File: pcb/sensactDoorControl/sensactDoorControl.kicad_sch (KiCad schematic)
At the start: 51 parts, among them J1 Conn_01x04, J10 Conn_01x06, J11 G19, J12 G23, J2 Conn_01x04, J3 Motor, J4 PROG, J5 Conn_01x04, J6 Conn_01x04, J7 G2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

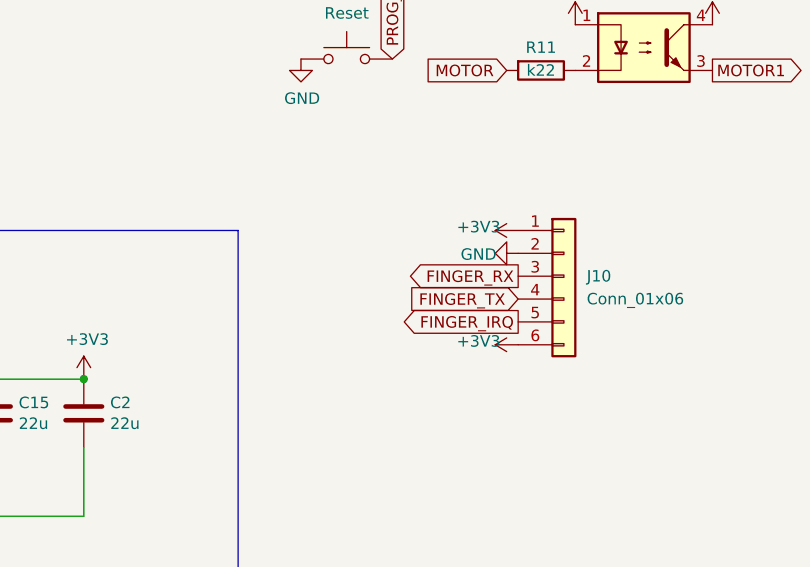
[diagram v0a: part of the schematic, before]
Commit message: sh connector with jumper
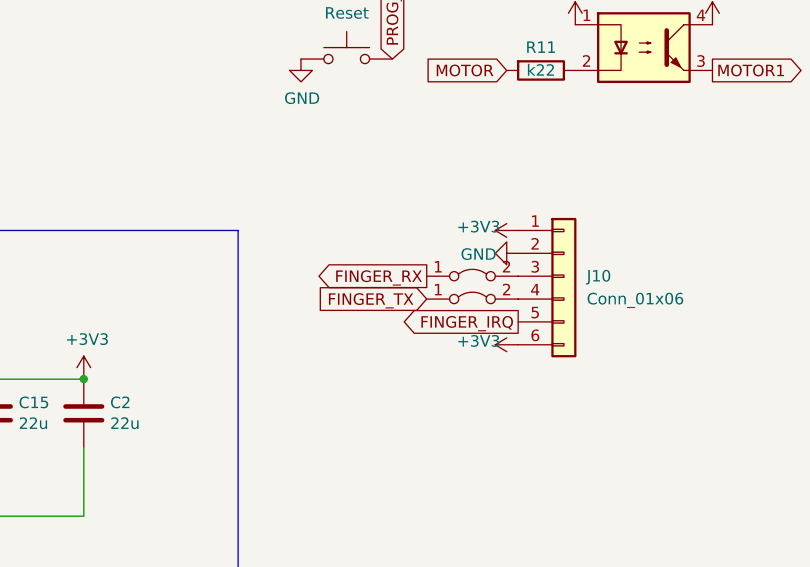
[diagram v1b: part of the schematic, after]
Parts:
- added JP1, JP2: Jumper_2_Bridged, Jumper:SolderJumper-2_P1.3mm_Bridged_RoundedPad1.0x1.5mm, symbol Jumper:Jumper_2_Bridged
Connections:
- net FINGER_RX: now also JP1.1 (A); no longer J10.3 (Pin_3)
- net FINGER_TX: now also JP2.1 (A); no longer J10.4 (Pin_4)
- new net: J10.3 (Pin_3), JP1.2 (B)
- new net: J10.4 (Pin_4), JP2.2 (B)
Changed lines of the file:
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@@
     )
   )
-  (global_label "FINGER_RX" (shape output) (at 153.67 151.13 180) (fields_autoplaced)
+  (global_label "FINGER_RX" (shape output) (at 143.51 151.13 180) (fields_autoplaced)
     (effects (font (size 1.27 1.27)) (justify right))
-    (property "Intersheetrefs" "${INTERSHEET_REFS}" (at 140.5248 151.13 0)
+    (property "Intersheetrefs" "${INTERSHEET_REFS}" (at 130.3648 151.13 0)
       (effects (font (size 1.27 1.27)) (justify right) hide)
     )
@@
     )
   )
-  (global_label "FINGER_TX" (shape input) (at 153.67 153.67 180) (fields_autoplaced)
+  (global_label "FINGER_TX" (shape input) (at 143.51 153.67 180) (fields_autoplaced)
     (effects (font (size 1.27 1.27)) (justify right))
-    (property "Intersheetrefs" "${INTERSHEET_REFS}" (at 140.8272 153.67 0)
+    (property "Intersheetrefs" "${INTERSHEET_REFS}" (at 130.6672 153.67 0)
       (effects (font (size 1.27 1.27)) (justify right) hide)
     )
@@
     )
   )
+  (symbol (lib_id "Jumper:Jumper_2_Bridged") (at 148.59 151.13 0) (unit 1)
+    (in_bom yes) (on_board yes) (dnp no) (fields_autoplaced)
+    (property "Reference" "JP1" (at 148.59 146.05 0)
+      (effects (font (size 1.27 1.27)) hide)
+    )
+    (property "Value" "Jumper_2_Bridged" (at 148.59 148.59 0)
+      (effects (font (size 1.27 1.27)) hide)
+    )
+    (property "Footprint" "Jumper:SolderJumper-2_P1.3mm_Bridged_RoundedPad1.0x1.5mm" (at 148.59 151.13 0)
+      (effects (font (size 1.27 1.27)) hide)
+    )
+    (property "Datasheet" "~" (at 148.59 151.13 0)
+      (effects (font (size 1.27 1.27)) hide)
+    )
+    (pin "2")
+    (pin "1")
+    (instances
+      (project "sensactDoorControl"
+        (path "/43f0baf2-6f79-4cf2-88c1-5a3cf0eb3b7b"
+          (reference "JP1") (unit 1)
+        )
+      )
+    )
+  )
   (symbol (lib_id "Device:R") (at 91.44 166.37 0) (unit 1)
     (in_bom yes) (on_board yes) (dnp no)
@@
         )
       )
+    )
+  )
+  (symbol (lib_id "Jumper:Jumper_2_Bridged") (at 148.59 153.67 0) (unit 1)
+    (in_bom yes) (on_board yes) (dnp no) (fields_autoplaced)
+    (property "Reference" "JP2" (at 148.59 148.59 0)
+      (effects (font (size 1.27 1.27)) hide)
+    )
+    (property "Value" "Jumper_2_Bridged" (at 148.59 151.13 0)
+      (effects (font (size 1.27 1.27)) hide)
+    )
+    (property "Footprint" "Jumper:SolderJumper-2_P1.3mm_Bridged_RoundedPad1.0x1.5mm" (at 148.59 153.67 0)
+      (effects (font (size 1.27 1.27)) hide)
+    )
+    (property "Datasheet" "~" (at 148.59 153.67 0)
+      (effects (font (size 1.27 1.27)) hide)
+    )
+    (pin "2")
+    (pin "1")
+    (instances
+      (project "sensactDoorControl"
+        (path "/43f0baf2-6f79-4cf2-88c1-5a3cf0eb3b7b"
+          (reference "JP2") (unit 1)
+        )
+      )

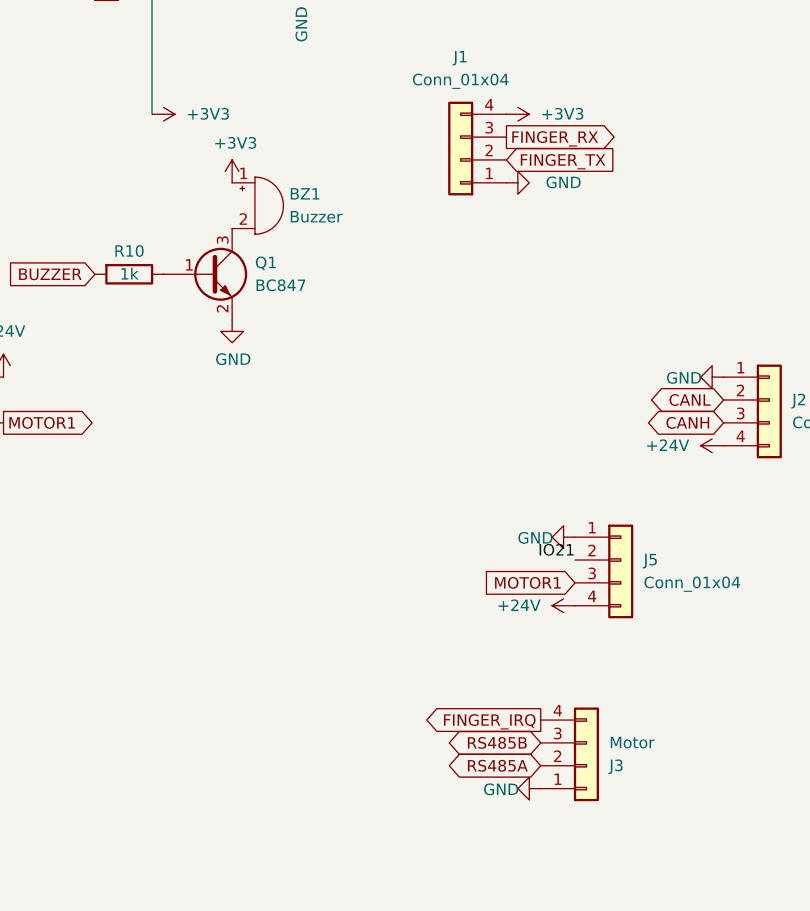
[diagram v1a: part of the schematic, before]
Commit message: Improved layout sensactDoorControl
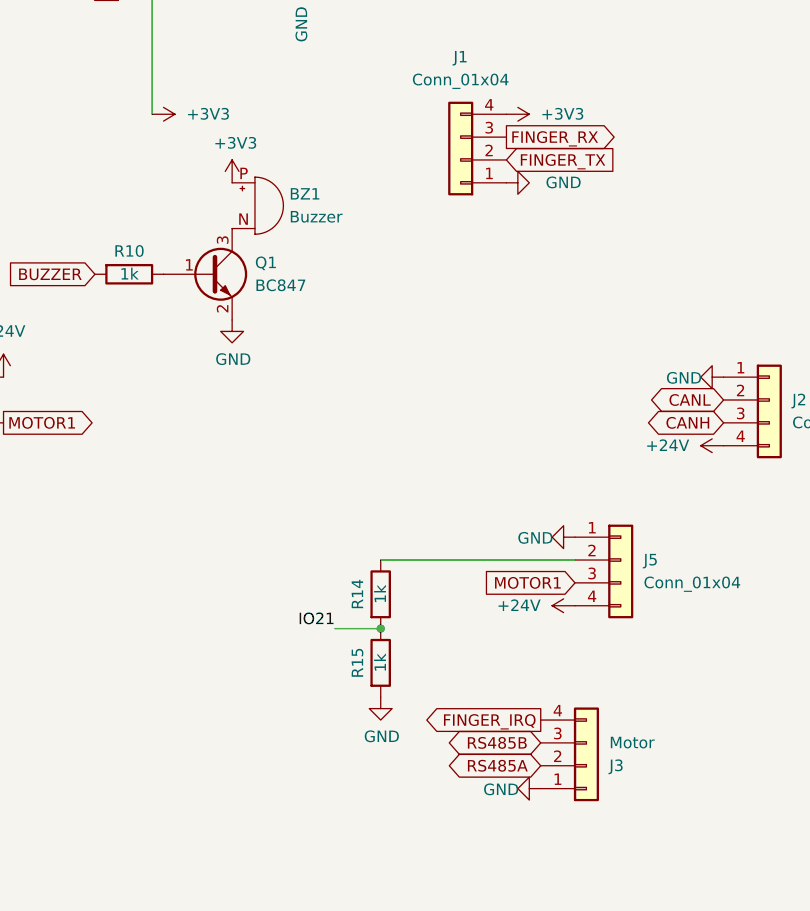
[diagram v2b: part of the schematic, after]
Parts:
- removed BZ1: Buzzer, Buzzer_Beeper:Buzzer_12x9.5RM7.6, symbol Device:Buzzer
- added BZ1: Buzzer, liebler_MECH:XDCR_CMT-7525-80-SMT-TR_handsolder, symbol liebler_MECH:Buzzer
- added R14, R15: 1k, Resistor_SMD:R_0805_2012Metric_Pad1.20x1.40mm_HandSolder, symbol Device:R
- JP1: value Jumper_2_Bridged -> RX
- JP2: value Jumper_2_Bridged -> TX
- SW1, SW2: footprint Button_Switch_SMD:SW_Push_1P1T_NO_6x6mm_H9.5mm -> liebler_MECH:SW_SPST_TL3342_smaller_handsolder
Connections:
- net +3V3: now also BZ1.P (+)
- net GND: now also R15.2
- net IO21: now also R14.2, R15.1; no longer J5.2 (Pin_2)
- net at Q1.3 (C): now also BZ1.N (-)
- new net: J5.2 (Pin_2), R14.1
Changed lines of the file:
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@@
   (junction (at 151.13 77.47) (diameter 0) (color 0 0 0 0)
+  )
+  (junction (at 217.17 151.13) (diameter 0) (color 0 0 0 0)
   )
   (junction (at 83.82 170.18) (diameter 0) (color 0 0 0 0)
@@
     (stroke (width 0) (type default))
   )
+  (wire (pts (xy 212.09 151.13) (xy 217.17 151.13))
+    (stroke (width 0) (type default))
+  )
   (wire (pts (xy 95.25 177.8) (xy 91.44 177.8))
     (stroke (width 0) (type default))
@@
   )
   (wire (pts (xy 95.25 170.18) (xy 95.25 177.8))
+    (stroke (width 0) (type default))
+  )
+  (wire (pts (xy 217.17 143.51) (xy 238.76 143.51))
     (stroke (width 0) (type default))
   )
@@
     (effects (font (size 1.27 1.27)) (justify right bottom))
   )
-  (label "IO21" (at 238.76 143.51 180) (fields_autoplaced)
+  (label "IO21" (at 212.09 151.13 180) (fields_autoplaced)
     (effects (font (size 1.27 1.27)) (justify right bottom))
   )
@@
         (path "/43f0baf2-6f79-4cf2-88c1-5a3cf0eb3b7b"
           (reference "R7") (unit 1)
-        )
-      )
-    )
-  )
-  (symbol (lib_id "Device:Buzzer") (at 203.2 104.14 0) (unit 1)
-    (in_bom yes) (on_board yes) (dnp no) (fields_autoplaced)
-    (property "Reference" "BZ1" (at 207.01 102.87 0)
-      (effects (font (size 1.27 1.27)) (justify left))
-    )
-    (property "Value" "Buzzer" (at 207.01 105.41 0)
-      (effects (font (size 1.27 1.27)) (justify left))
-    )
-    (property "Footprint" "Buzzer_Beeper:Buzzer_12x9.5RM7.6" (at 202.565 101.6 90)
-      (effects (font (size 1.27 1.27)) hide)
-    )
-    (property "Datasheet" "~" (at 202.565 101.6 90)
-      (effects (font (size 1.27 1.27)) hide)
-    )
-    (pin "1")
-    (pin "2")
-    (instances
-      (project "sensactDoorControl"
-        (path "/43f0baf2-6f79-4cf2-88c1-5a3cf0eb3b7b"
-          (reference "BZ1") (unit 1)
         )
       )
@@
     )
   )
+  (symbol (lib_id "Device:R") (at 217.17 154.94 0) (unit 1)
+    (in_bom yes) (on_board yes) (dnp no)
+    (property "Reference" "R15" (at 214.63 154.94 90)
+      (effects (font (size 1.27 1.27)))
+    )
+    (property "Value" "1k" (at 217.17 154.94 90)
+      (effects (font (size 1.27 1.27)))
+    )
+    (property "Footprint" "Resistor_SMD:R_0805_2012Metric_Pad1.20x1.40mm_HandSolder" (at 215.392 154.94 90)
+      (effects (font (size 1.27 1.27)) hide)
+    )
+    (property "Datasheet" "~" (at 217.17 154.94 0)
+      (effects (font (size 1.27 1.27)) hide)
+    )
+    (pin "1")
+    (pin "2")
+    (instances
+      (project "sensactDoorControl"
+        (path "/43f0baf2-6f79-4cf2-88c1-5a3cf0eb3b7b"
+          (reference "R15") (unit 1)
+        )
+      )
+    )
+  )
   (symbol (lib_id "power:GND") (at 200.66 116.84 0) (unit 1)
     (in_bom yes) (on_board yes) (dnp no)
@@
       (effects (font (size 1.27 1.27)))
     )
-    (property "Footprint" "Button_Switch_SMD:SW_Push_1P1T_NO_6x6mm_H9.5mm" (at 134.62 121.92 0)
+    (property "Footprint" "liebler_MECH:SW_SPST_TL3342_smaller_handsolder" (at 134.62 121.92 0)
       (effects (font (size 1.27 1.27)) hide)
     )
@@
       (effects (font (size 1.27 1.27)) hide)
     )
-    (property "Value" "Jumper_2_Bridged" (at 148.59 148.59 0)
+    (property "Value" "RX" (at 148.59 148.59 0)
       (effects (font (size 1.27 1.27)) hide)
     )
@@
     )
   )
+  (symbol (lib_id "liebler_MECH:Buzzer") (at 203.2 104.14 0) (unit 1)
+    (in_bom yes) (on_board yes) (dnp no) (fields_autoplaced)
+    (property "Reference" "BZ1" (at 207.01 102.87 0)
+      (effects (font (size 1.27 1.27)) (justify left))
+    )
+    (property "Value" "Buzzer" (at 207.01 105.41 0)
+      (effects (font (size 1.27 1.27)) (justify left))
+    )
+    (property "Footprint" "liebler_MECH:XDCR_CMT-7525-80-SMT-TR_handsolder" (at 202.565 101.6 90)
+      (effects (font (size 1.27 1.27)) hide)
+    )
+    (property "Datasheet" "~" (at 202.565 101.6 90)
+      (effects (font (size 1.27 1.27)) hide)
+    )
+    (pin "P")
+    (pin "N")
+    (instances
+      (project "sensactDoorControl"
+        (path "/43f0baf2-6f79-4cf2-88c1-5a3cf0eb3b7b"
+          (reference "BZ1") (unit 1)
+        )
+      )
+    )
+  )
   (symbol (lib_id "power:+3V3") (at 153.67 146.05 90) (unit 1)
     (in_bom yes) (on_board yes) (dnp no)
@@
         (path "/43f0baf2-6f79-4cf2-88c1-5a3cf0eb3b7b"
           (reference "#PWR045") (unit 1)
+        )
+      )
+    )
+  )
+  (symbol (lib_id "power:GND") (at 217.17 158.75 0) (unit 1)
+    (in_bom yes) (on_board yes) (dnp no)
+    (property "Reference" "#PWR048" (at 217.17 165.1 0)
+      (effects (font (size 1.27 1.27)) hide)
+    )
+    (property "Value" "GND" (at 217.297 163.1442 0)
+      (effects (font (size 1.27 1.27)))
+    )
+    (property "Footprint" "" (at 217.17 158.75 0)
+      (effects (font (size 1.27 1.27)) hide)
+    )
+    (property "Datasheet" "" (at 217.17 158.75 0)
+      (effects (font (size 1.27 1.27)) hide)
+    )
+    (pin "1")
+    (instances
+      (project "sensactDoorControl"
+        (path "/43f0baf2-6f79-4cf2-88c1-5a3cf0eb3b7b"
+          (reference "#PWR048") (unit 1)
         )
       )
@@
       (effects (font (size 1.27 1.27)))
     )
-    (property "Footprint" "Button_Switch_SMD:SW_Push_1P1T_NO_6x6mm_H9.5mm" (at 134.62 109.22 0)
+    (property "Footprint" "liebler_MECH:SW_SPST_TL3342_smaller_handsolder" (at 134.62 109.22 0)
       (effects (font (size 1.27 1.27)) hide)
     )
@@
       (effects (font (size 1.27 1.27)) hide)
     )
-    (property "Value" "Jumper_2_Bridged" (at 148.59 151.13 0)
+    (property "Value" "TX" (at 148.59 151.13 0)
       (effects (font (size 1.27 1.27)) hide)
     )
@@
         )
       )
+    )
+  )
+  (symbol (lib_id "Device:R") (at 217.17 147.32 0) (unit 1)
+    (in_bom yes) (on_board yes) (dnp no)
+    (property "Reference" "R14" (at 214.63 147.32 90)
+      (effects (font (size 1.27 1.27)))
+    )
+    (property "Value" "1k" (at 217.17 147.32 90)
+      (effects (font (size 1.27 1.27)))
+    )
+    (property "Footprint" "Resistor_SMD:R_0805_2012Metric_Pad1.20x1.40mm_HandSolder" (at 215.392 147.32 90)
+      (effects (font (size 1.27 1.27)) hide)
+    )
+    (property "Datasheet" "~" (at 217.17 147.32 0)
+      (effects (font (size 1.27 1.27)) hide)
+    )
+    (pin "1")
+    (pin "2")
+    (instances
+      (project "sensactDoorControl"
+        (path "/43f0baf2-6f79-4cf2-88c1-5a3cf0eb3b7b"
+          (reference "R14") (unit 1)
+        )
+      )

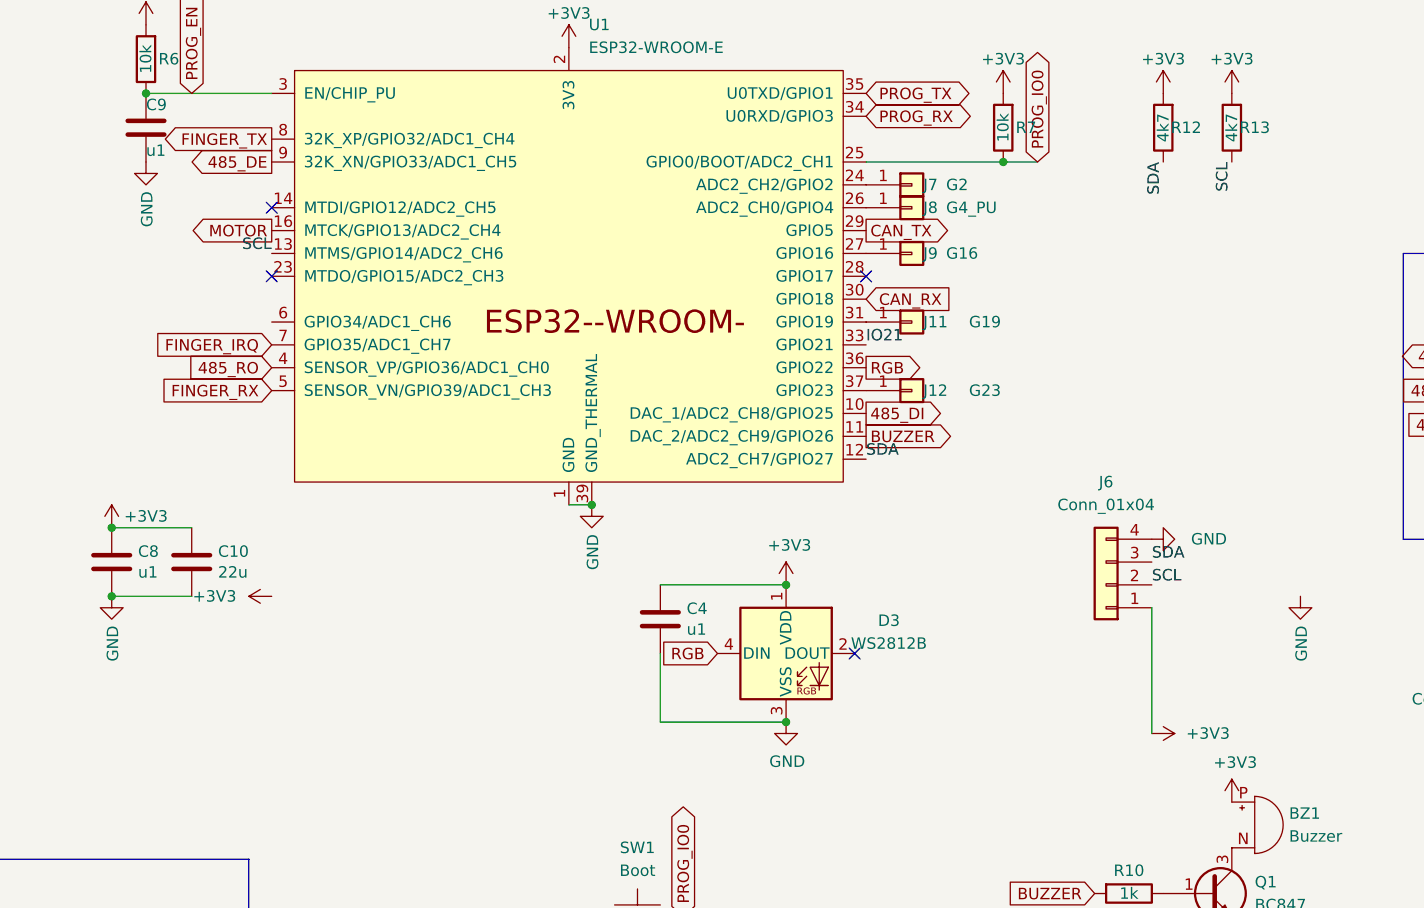
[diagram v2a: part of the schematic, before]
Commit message: larger i2c mith io pins
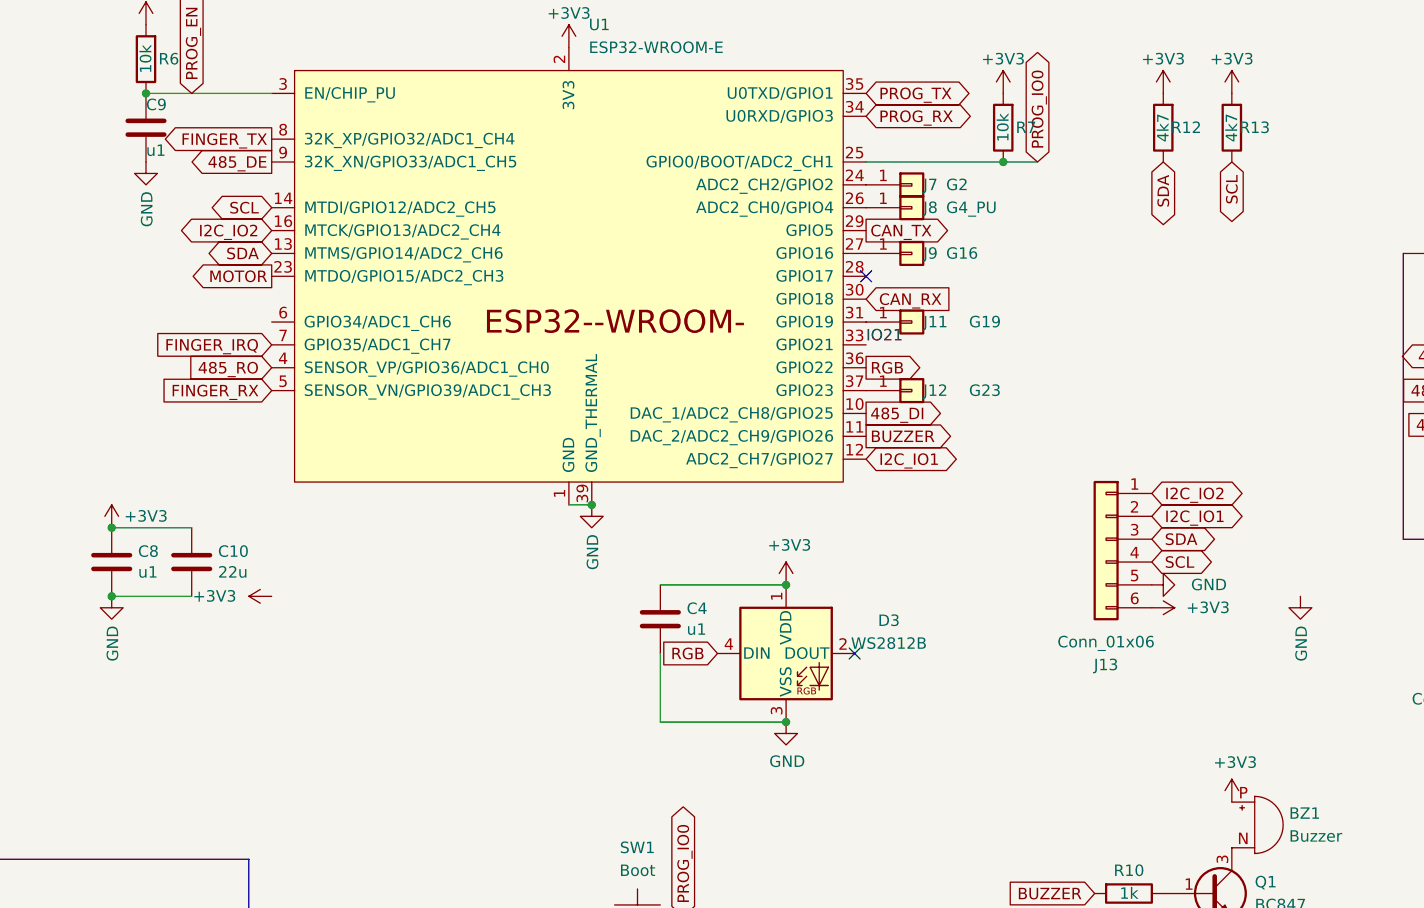
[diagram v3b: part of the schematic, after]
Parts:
- removed J6: Conn_01x04, Connector_JST:JST_XH_B4B-XH-A_1x04_P2.50mm_Vertical, symbol Connector_Generic:Conn_01x04
- added J13: Conn_01x06, Connector_JST:JST_XH_B6B-XH-A_1x06_P2.50mm_Vertical, symbol Connector_Generic:Conn_01x06
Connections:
- net +3V3: now also J13.6 (Pin_6)
- net GND: now also J13.5 (Pin_5)
- net MOTOR: now also U1.23 (MTDO/GPIO15/ADC2_CH3); no longer U1.16 (MTCK/GPIO13/ADC2_CH4)
- net SCL: now also U1.14 (MTDI/GPIO12/ADC2_CH5), J13.4 (Pin_4); no longer U1.13 (MTMS/GPIO14/ADC2_CH6)
- net SDA: now also U1.13 (MTMS/GPIO14/ADC2_CH6), J13.3 (Pin_3); no longer U1.12 (ADC2_CH7/GPIO27)
- new net I2C_IO1: J13.2 (Pin_2), U1.12 (ADC2_CH7/GPIO27)
- new net I2C_IO2: J13.1 (Pin_1), U1.16 (MTCK/GPIO13/ADC2_CH4)
- no-connect marks 6 -> 4

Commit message: sensactDoorCtrl PCB as ordered @JLCPCB
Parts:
- removed J7: G2, TestPoint:TestPoint_THTPad_D1.5mm_Drill0.7mm, symbol Connector_Generic:Conn_01x01
- J1: value Conn_01x04 -> Finger_large
- J10: value Conn_01x06 -> Fingerprint; footprint Connector_JST:JST_SH_SM06B-SRSS-TB_1x06-1MP_P1.00mm_Horizontal -> liebler_CONN:JST_SH_SM06B-SRSS-TB_1x06-1MP_P1.00mm_Horizontal_handsolder
- J13: value Conn_01x06 -> I2C
- J2: value Conn_01x04 -> Can+24V
- J3: value Motor -> RS485
- J5: value Conn_01x04 -> Motor
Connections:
- no-connect marks 4 -> 5
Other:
- moved on the sheet: J1, J10, J2, J3, J5, R14, R15
